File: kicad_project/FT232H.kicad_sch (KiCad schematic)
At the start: 1 part, among them U10 FT232H

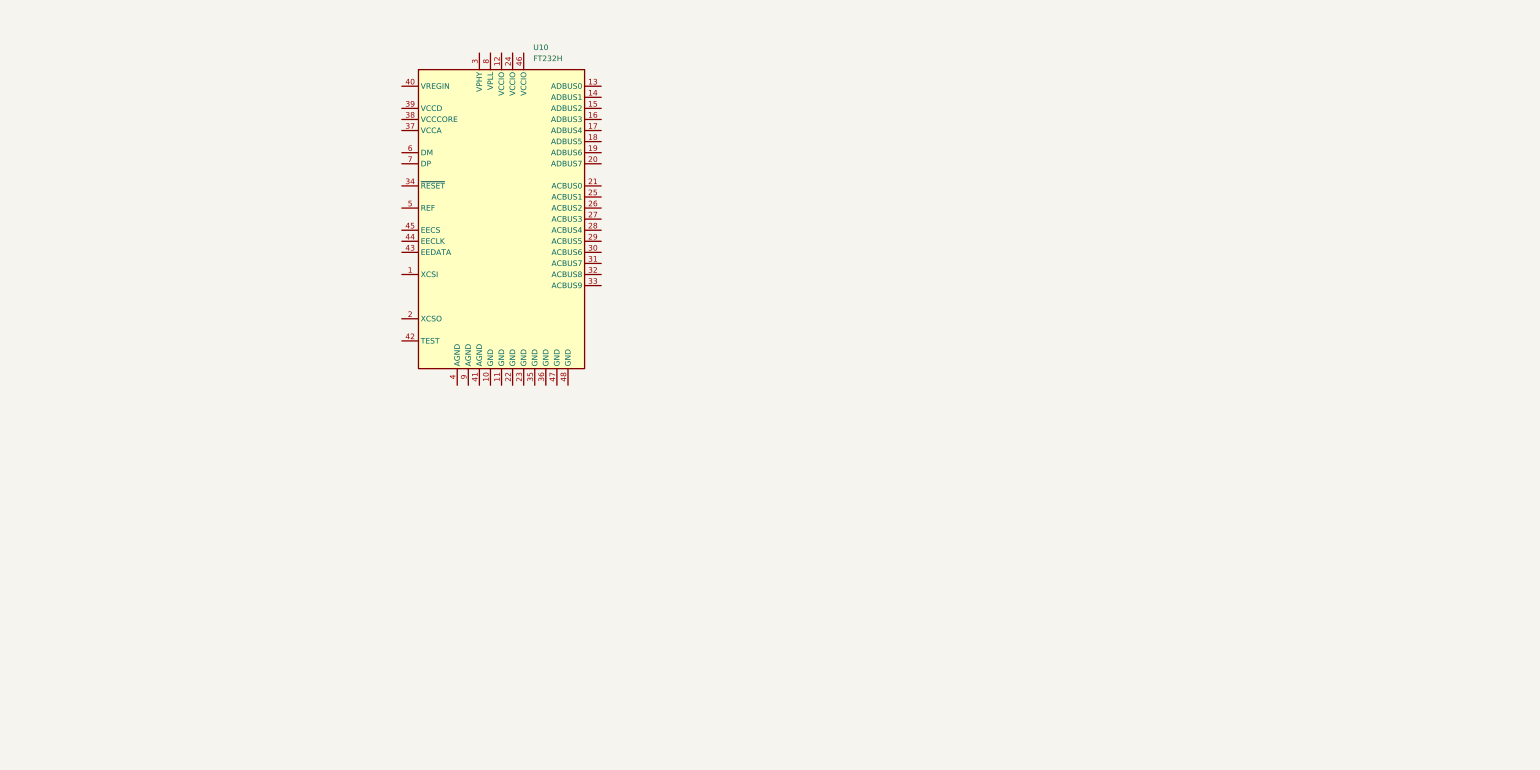
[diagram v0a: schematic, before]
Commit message: Start on FT232H sheet
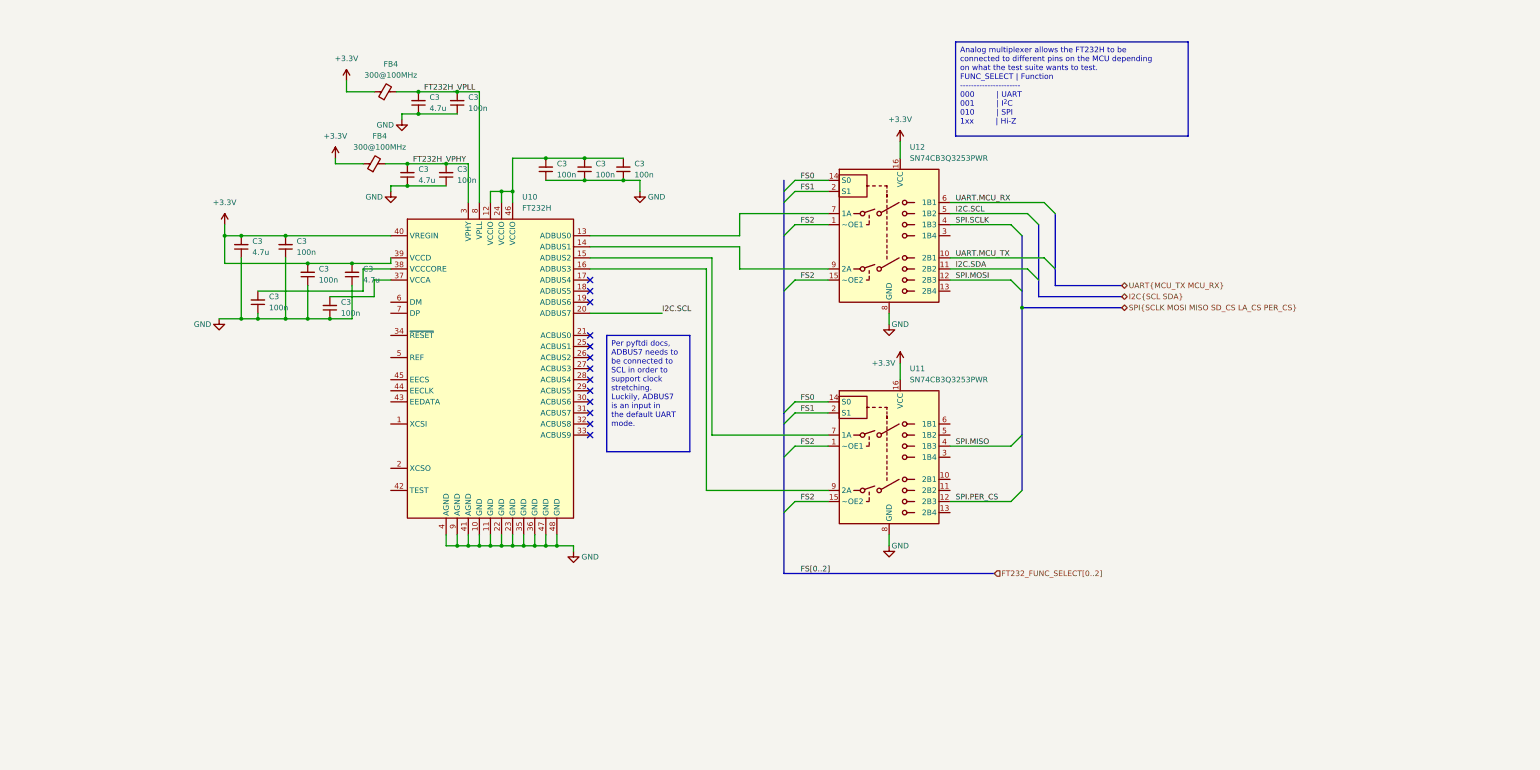
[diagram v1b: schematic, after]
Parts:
- added C3 (x4): 4.7u, Capacitor_SMD:C_1206_3216Metric, symbol Device:C_Small
- added C3 (x9): 100n, Capacitor_SMD:C_1206_3216Metric, symbol Device:C_Small
- added FB4 (x2): 300@100MHz, Resistor_SMD:R_1206_3216Metric, symbol Device:FerriteBead_Small
- added U11, U12: SN74CB3Q3253PWR, Package_SO:TSSOP-16_4.4x5mm_P0.65mm, symbol project libraries:SN74CB3Q3253PWR
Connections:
- net GND: now reaches U10.10 (GND)
- net GND: now also U10.11 (GND), U10.22 (GND), U10.23 (GND), U10.35 (GND), U10.36 (GND), U10.4 (AGND), U10.41 (AGND), U10.47 (GND), U10.48 (GND), U10.9 (AGND), C3.1, C3.1, C3.1, C3.1, C3.1, C3.1, C3.1, C3.1, C3.1, C3.1, C3.1, C3.1, C3.1, U11.8 (GND), U12.8 (GND)
- net at U10.12 (VCCIO): now also U10.24 (VCCIO), U10.46 (VCCIO), C3.2, C3.2, C3.2
- net at U10.13 (ADBUS0): now also U12.7 (1A)
- net at U10.14 (ADBUS1): now also U12.9 (2A)
- net at U10.15 (ADBUS2): now also U11.7 (1A)
- net at U10.16 (ADBUS3): now also U11.9 (2A)
- net I2C.SCL: now reaches U10.20 (ADBUS7)
- net I2C.SCL: now also U12.5 (1B2)
- net FT232H_VPHY: now reaches U10.3 (VPHY)
- net FT232H_VPHY: now also C3.2, C3.2, FB4.2
- net at U10.37 (VCCA): now also C3.2
- net at U10.38 (VCCCORE): now also C3.2
- net +3.3V: now reaches U10.39 (VCCD)
- net +3.3V: now also U10.40 (VREGIN), C3.2, C3.2, C3.2, C3.2, FB4.1, FB4.1, U11.16 (VCC), U12.16 (VCC)
- net FT232H_VPLL: now reaches U10.8 (VPLL)
- net FT232H_VPLL: now also C3.2, C3.2, FB4.2
- new net FS0: U11.14 (S0), U12.14 (S0)
- new net FS1: U11.2 (S1), U12.2 (S1)
- new net FS2: U11.1 (~OE1), U11.15 (~OE2), U12.1 (~OE1), U12.15 (~OE2)
- new net I2C.SDA: U12.11 (2B2)
- new net SPI.MISO: U11.4 (1B3)
- new net SPI.MOSI: U12.12 (2B3)
- new net SPI.PER_CS: U11.12 (2B3)
- new net SPI.SCLK: U12.4 (1B3)
- new net UART.MCU_RX: U12.6 (1B1)
- new net UART.MCU_TX: U12.10 (2B1)
- no-connect marks 0 -> 13
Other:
- moved on the sheet: U10

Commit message: Add arduino shield schematic, finish FT232H
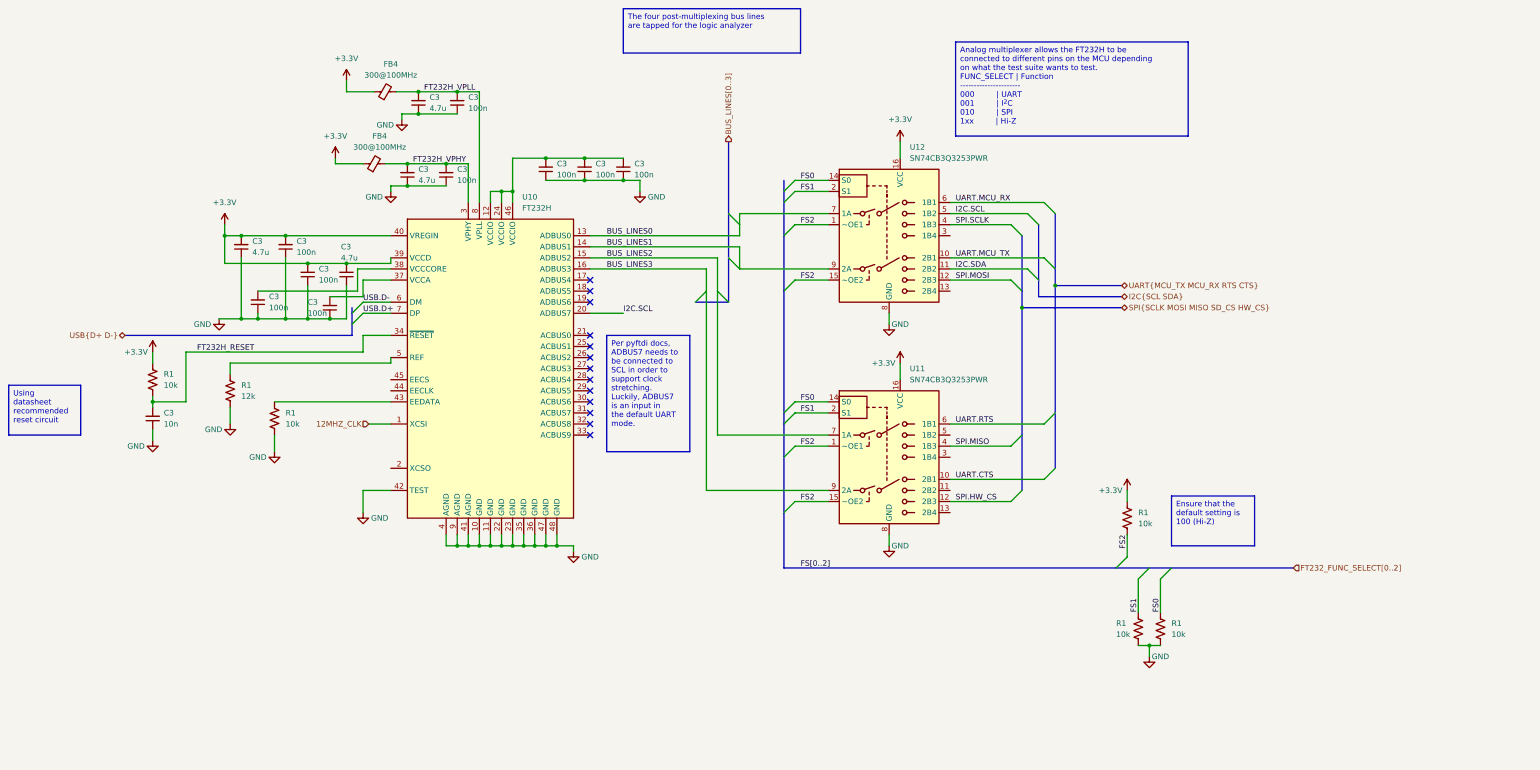
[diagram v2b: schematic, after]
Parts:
- added C3: 10n, Capacitor_SMD:C_1206_3216Metric, symbol Device:C_Small
- added R1 (x5): 10k, Resistor_SMD:R_1206_3216Metric, symbol Device:R_US
- added R1: 12k, Resistor_SMD:R_1206_3216Metric, symbol Device:R_US
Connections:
- net +3.3V: now also R1.1, R1.1
- net FS0: now also R1.1
- net FS1: now also R1.1
- net FS2: now also R1.2
- net GND: now also U10.42 (TEST), C3.1, R1.2, R1.2, R1.2, R1.2
- net BUS_LINES0: now reaches U10.13 (ADBUS0), U12.7 (1A)
- net BUS_LINES1: now reaches U10.14 (ADBUS1), U12.9 (2A)
- net UART.CTS: now reaches U11.10 (2B1)
- net UART.RTS: now reaches U11.6 (1B1)
- net BUS_LINES2: now reaches U10.15 (ADBUS2), U11.7 (1A)
- net BUS_LINES3: now reaches U10.16 (ADBUS3), U11.9 (2A)
- net 12MHZ_CLK: now reaches U10.1 (XCSI)
- net FT232H_RESET: now reaches U10.34 (~{RESET})
- net FT232H_RESET: now also C3.2, R1.2
- net at U10.43 (EEDATA): now also R1.1
- net at U10.5 (REF): now also R1.1
- net USB.D-: now reaches U10.6 (DM)
- net USB.D+: now reaches U10.7 (DP)
- net SPI.PER_CS renamed SPI.HW_CS
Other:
- moved on the sheet: C3

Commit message: Finish up initial schematic
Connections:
- net +3.3V: now also C3.2, C3.2, C3.2, U10.12 (VCCIO), U10.24 (VCCIO), U10.46 (VCCIO)
- net FS0 renamed FT232_FUNC_SELECT0
- net FS1 renamed FT232_FUNC_SELECT1
- net FS2 renamed FT232_FUNC_SELECT2
- no-connect marks 13 -> 22
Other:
- moved on the sheet: R1, U11, U12

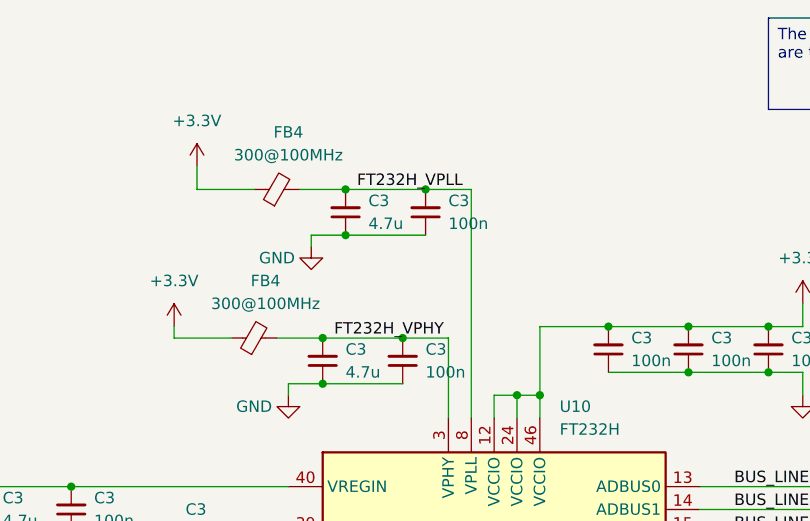
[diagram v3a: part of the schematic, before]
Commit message: Add logo to PCB, add last labels, fix DRC
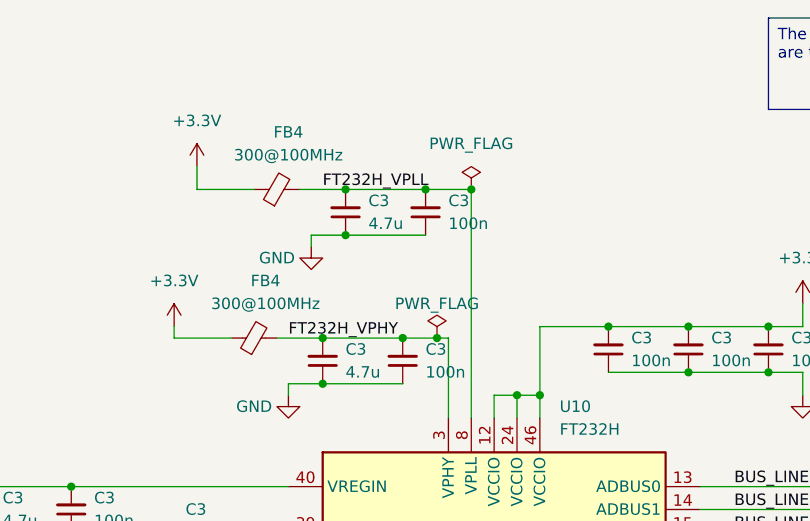
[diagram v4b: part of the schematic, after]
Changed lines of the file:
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@@
   (junction (at 134.62 165.1) (diameter 0) (color 0 0 0 0)
   )
+  (junction (at 124.46 60.96) (diameter 0) (color 0 0 0 0)
+  )
   (junction (at 129.54 83.82) (diameter 0) (color 0 0 0 0)
+  )
+  (junction (at 120.65 77.47) (diameter 0) (color 0 0 0 0)
   )
   (junction (at 142.24 165.1) (diameter 0) (color 0 0 0 0)
@@
     (stroke (width 0) (type default))
   )
+  (wire (pts (xy 110.49 60.96) (xy 119.38 60.96))
+    (stroke (width 0) (type default))
+  )
   (wire (pts (xy 299.72 209.55) (xy 302.26 209.55))
     (stroke (width 0) (type default))
   )
+  (wire (pts (xy 102.87 77.47) (xy 107.95 77.47))
+    (stroke (width 0) (type default))
+  )
   (bus (pts (xy 194.31 93.98) (xy 194.31 106.68))
     (stroke (width 0) (type default))
@@
     (stroke (width 0) (type default))
   )
-  (wire (pts (xy 116.84 77.47) (xy 121.92 77.47))
+  (wire (pts (xy 116.84 77.47) (xy 120.65 77.47))
     (stroke (width 0) (type default))
   )
@@
     (stroke (width 0) (type default))
   )
+  (wire (pts (xy 67.31 133.35) (xy 67.31 137.16))
+    (stroke (width 0) (type default))
+  )
+  (wire (pts (xy 121.92 165.1) (xy 124.46 165.1))
+    (stroke (width 0) (type default))
+  )
+  (wire (pts (xy 121.92 162.56) (xy 121.92 165.1))
+    (stroke (width 0) (type default))
+  )
+  (wire (pts (xy 77.47 132.08) (xy 104.14 132.08))
+    (stroke (width 0) (type default))
+  )
+  (wire (pts (xy 137.16 162.56) (xy 137.16 165.1))
+    (stroke (width 0) (type default))
+  )
+  (wire (pts (xy 297.18 133.35) (xy 297.18 135.89))
+    (stroke (width 0) (type default))
+  )
+  (wire (pts (xy 196.85 81.28) (xy 228.6 81.28))
+    (stroke (width 0) (type default))
+  )
+  (wire (pts (xy 299.72 172.72) (xy 299.72 201.93))
+    (stroke (width 0) (type default))
+  )
+  (wire (pts (xy 149.86 96.52) (xy 184.15 96.52))
+    (stroke (width 0) (type default))
+  )
+  (wire (pts (xy 105.41 60.96) (xy 110.49 60.96))
+    (stroke (width 0) (type default))
+  )
+  (wire (pts (xy 93.98 60.96) (xy 93.98 58.42))
+    (stroke (width 0) (type default))
+  )
+  (wire (pts (xy 137.16 165.1) (xy 139.7 165.1))
+    (stroke (width 0) (type default))
+  )
+  (bus (pts (xy 280.67 134.62) (xy 280.67 147.32))
+    (stroke (width 0) (type default))
+  )
+  (wire (pts (xy 91.44 77.47) (xy 91.44 76.2))
+    (stroke (width 0) (type default))
+  )
+  (bus (pts (xy 295.91 105.41) (xy 280.67 105.41))
+    (stroke (width 0) (type default))
+  )
+  (wire (pts (xy 129.54 162.56) (xy 129.54 165.1))
+    (stroke (width 0) (type default))
+  )
+  (wire (pts (xy 127 162.56) (xy 127 165.1))
+    (stroke (width 0) (type default))
+  )
+  (wire (pts (xy 179.07 106.68) (xy 179.07 139.7))
+    (stroke (width 0) (type default))
+  )
+  (wire (pts (xy 139.7 81.28) (xy 148.59 81.28))
+    (stroke (width 0) (type default))
+  )
+  (wire (pts (xy 96.52 101.6) (xy 96.52 106.68))
+    (stroke (width 0) (type default))
+  )
+  (wire (pts (xy 132.08 83.82) (xy 132.08 86.36))
+    (stroke (width 0) (type default))
+  )
+  (wire (pts (xy 80.01 93.98) (xy 69.85 93.98))
+    (stroke (width 0) (type default))
+  )
+  (wire (pts (xy 139.7 76.2) (xy 132.08 76.2))
+    (stroke (width 0) (type default))
+  )
+  (bus (pts (xy 95.25 110.49) (xy 95.25 111.76))
+    (stroke (width 0) (type default))
+  )
+  (bus (pts (xy 95.25 114.3) (xy 95.25 116.84))
+    (stroke (width 0) (type default))
+  )
+  (wire (pts (xy 148.59 76.2) (xy 139.7 76.2))
+    (stroke (width 0) (type default))
+  )
   (wire (pts (xy 107.95 77.47) (xy 116.84 77.47))
     (stroke (width 0) (type default))
   )
-  (wire (pts (xy 67.31 133.35) (xy 67.31 137.16))
-    (stroke (width 0) (type default))
-  )
-  (wire (pts (xy 121.92 165.1) (xy 124.46 165.1))
-    (stroke (width 0) (type default))
-  )
-  (wire (pts (xy 121.92 162.56) (xy 121.92 165.1))
-    (stroke (width 0) (type default))
-  )
-  (wire (pts (xy 77.47 132.08) (xy 104.14 132.08))
-    (stroke (width 0) (type default))
-  )
-  (wire (pts (xy 137.16 162.56) (xy 137.16 165.1))
-    (stroke (width 0) (type default))
-  )
-  (wire (pts (xy 297.18 133.35) (xy 297.18 135.89))
-    (stroke (width 0) (type default))
-  )
-  (wire (pts (xy 196.85 81.28) (xy 228.6 81.28))
-    (stroke (width 0) (type default))
-  )
-  (wire (pts (xy 299.72 172.72) (xy 299.72 201.93))
-    (stroke (width 0) (type default))
-  )
-  (wire (pts (xy 149.86 96.52) (xy 184.15 96.52))
-    (stroke (width 0) (type default))
-  )
-  (wire (pts (xy 93.98 60.96) (xy 93.98 58.42))
-    (stroke (width 0) (type default))
-  )
-  (wire (pts (xy 137.16 165.1) (xy 139.7 165.1))
-    (stroke (width 0) (type default))
-  )
-  (bus (pts (xy 280.67 134.62) (xy 280.67 147.32))
-    (stroke (width 0) (type default))
-  )
-  (wire (pts (xy 91.44 77.47) (xy 91.44 76.2))
-    (stroke (width 0) (type default))
-  )
-  (bus (pts (xy 295.91 105.41) (xy 280.67 105.41))
-    (stroke (width 0) (type default))
-  )
-  (wire (pts (xy 129.54 162.56) (xy 129.54 165.1))
-    (stroke (width 0) (type default))
-  )
-  (wire (pts (xy 127 162.56) (xy 127 165.1))
-    (stroke (width 0) (type default))
-  )
-  (wire (pts (xy 179.07 106.68) (xy 179.07 139.7))
-    (stroke (width 0) (type default))
-  )
-  (wire (pts (xy 139.7 81.28) (xy 148.59 81.28))
-    (stroke (width 0) (type default))
-  )
-  (wire (pts (xy 96.52 101.6) (xy 96.52 106.68))
-    (stroke (width 0) (type default))
-  )
-  (wire (pts (xy 110.49 60.96) (xy 105.41 60.96))
-    (stroke (width 0) (type default))
-  )
-  (wire (pts (xy 132.08 83.82) (xy 132.08 86.36))
-    (stroke (width 0) (type default))
-  )
-  (wire (pts (xy 80.01 93.98) (xy 69.85 93.98))
-    (stroke (width 0) (type default))
-  )
-  (wire (pts (xy 139.7 76.2) (xy 132.08 76.2))
-    (stroke (width 0) (type default))
-  )
-  (bus (pts (xy 95.25 110.49) (xy 95.25 111.76))
-    (stroke (width 0) (type default))
-  )
-  (bus (pts (xy 95.25 114.3) (xy 95.25 116.84))
-    (stroke (width 0) (type default))
-  )
-  (wire (pts (xy 148.59 76.2) (xy 139.7 76.2))
-    (stroke (width 0) (type default))
-  )
   (wire (pts (xy 149.86 101.6) (xy 176.53 101.6))
     (stroke (width 0) (type default))
@@
     (stroke (width 0) (type default))
   )
-  (wire (pts (xy 102.87 77.47) (xy 107.95 77.47))
-    (stroke (width 0) (type default))
-  )
   (wire (pts (xy 69.85 99.06) (xy 69.85 113.03))
     (stroke (width 0) (type default))
@@
     (stroke (width 0) (type default))
   )
+  (wire (pts (xy 120.65 77.47) (xy 121.92 77.47))
+    (stroke (width 0) (type default))
+  )
   (bus (pts (xy 273.05 93.98) (xy 273.05 106.68))
     (stroke (width 0) (type default))
@@
   )
   (wire (pts (xy 196.85 154.94) (xy 228.6 154.94))
-    (stroke (width 0) (type default))
-  )
-  (wire (pts (xy 119.38 60.96) (xy 110.49 60.96))
     (stroke (width 0) (type default))
   )
@@
     (effects (font (face "Consolas") (size 1.27 1.27)) (justify left top))
   )
-  (label "FT232H_VPHY" (at 109.22 77.47 0) (fields_autoplaced)
+  (label "FT232H_VPHY" (at 104.14 77.47 0) (fields_autoplaced)
     (effects (font (size 1.27 1.27)) (justify left bottom))
   )
@@
     (effects (font (size 1.27 1.27)) (justify left bottom))
   )
-  (label "FT232H_VPLL" (at 111.76 60.96 0) (fields_autoplaced)
+  (label "FT232H_VPLL" (at 107.95 60.96 0) (fields_autoplaced)
     (effects (font (size 1.27 1.27)) (justify left bottom))
   )
@@
         (path "/a0f40274-9469-4bcf-885c-e8b8a490ea54/a2280405-5315-4fe3-be7c-fd34d4bf90fe"
           (reference "#PWR048") (unit 1)
+        )
+      )
+    )
+  )
+  (symbol (lib_id "power:PWR_FLAG") (at 120.65 77.47 0) (unit 1)
+    (in_bom yes) (on_board yes) (dnp no)
+    (property "Reference" "#FLG05" (at 120.65 75.565 0)
+      (effects (font (size 1.27 1.27)) hide)
+    )
+    (property "Value" "PWR_FLAG" (at 120.65 73.66 0)
+      (effects (font (size 1.27 1.27)))
+    )
+    (property "Footprint" "" (at 120.65 77.47 0)
+      (effects (font (size 1.27 1.27)) hide)
+    )
+    (property "Datasheet" "~" (at 120.65 77.47 0)
+      (effects (font (size 1.27 1.27)) hide)
+    )
+    (pin "1")
+    (instances
+      (project "mbed-ce-ci-shield-v2"
+        (path "/a0f40274-9469-4bcf-885c-e8b8a490ea54/d2cb7c4f-a03f-4f1c-8cab-0427a0ad2909"
+          (reference "#FLG05") (unit 1)
+        )
+        (path "/a0f40274-9469-4bcf-885c-e8b8a490ea54/a2280405-5315-4fe3-be7c-fd34d4bf90fe"
+          (reference "#FLG09") (unit 1)
         )
       )
@@
         )
       )
+    )
+  )
+  (symbol (lib_id "power:PWR_FLAG") (at 124.46 60.96 0) (unit 1)
+    (in_bom yes) (on_board yes) (dnp no) (fields_autoplaced)
+    (property "Reference" "#FLG05" (at 124.46 59.055 0)
+      (effects (font (size 1.27 1.27)) hide)
+    )
+    (property "Value" "PWR_FLAG" (at 124.46 55.88 0)
+      (effects (font (size 1.27 1.27)))
+    )
+    (property "Footprint" "" (at 124.46 60.96 0)
+      (effects (font (size 1.27 1.27)) hide)
+    )
+    (property "Datasheet" "~" (at 124.46 60.96 0)
+      (effects (font (size 1.27 1.27)) hide)
+    )
+    (pin "1")
+    (instances
+      (project "mbed-ce-ci-shield-v2"
+        (path "/a0f40274-9469-4bcf-885c-e8b8a490ea54/d2cb7c4f-a03f-4f1c-8cab-0427a0ad2909"
+          (reference "#FLG05") (unit 1)
+        )
+        (path "/a0f40274-9469-4bcf-885c-e8b8a490ea54/a2280405-5315-4fe3-be7c-fd34d4bf90fe"
+          (reference "#FLG08") (unit 1)
+        )
+      )
